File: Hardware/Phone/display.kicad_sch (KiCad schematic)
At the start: 19 parts, among them Q1 Si1308EDL

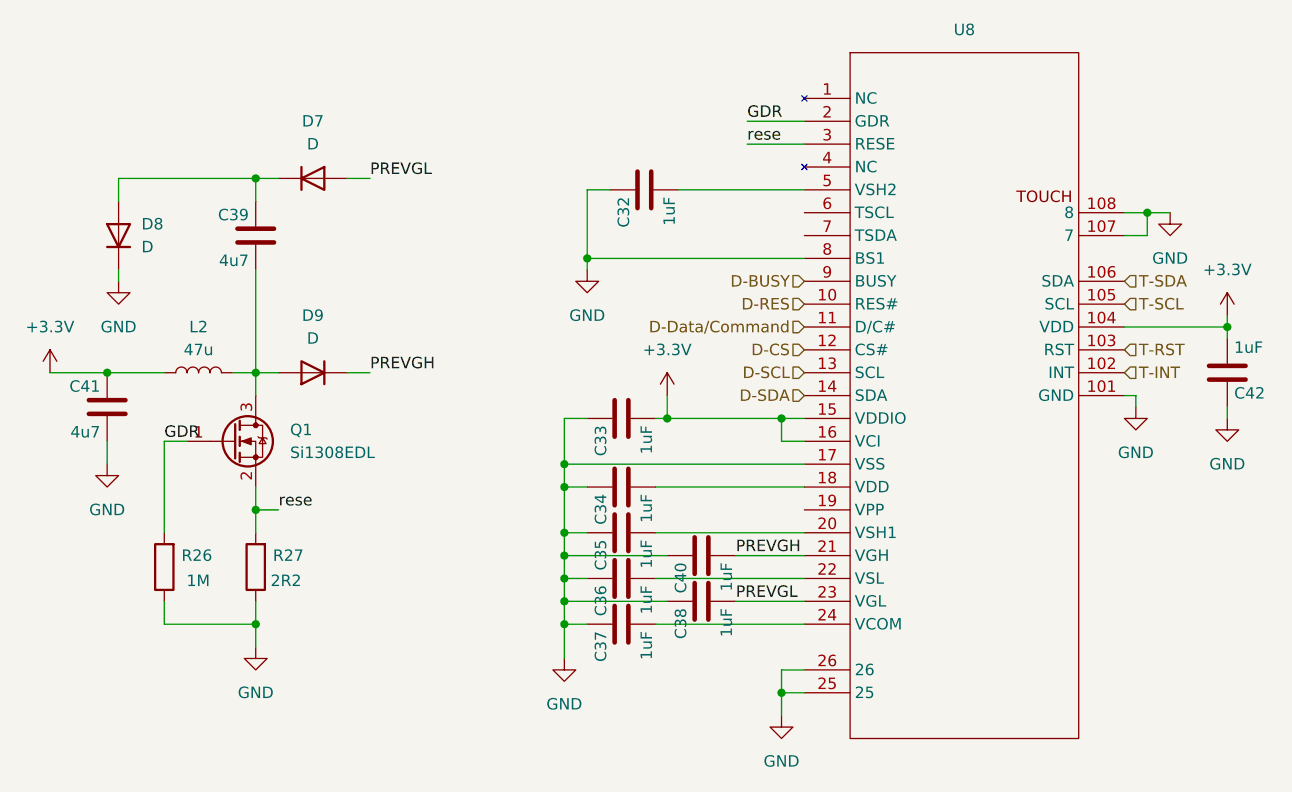
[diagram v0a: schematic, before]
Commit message: phone design is done abendoning projekt
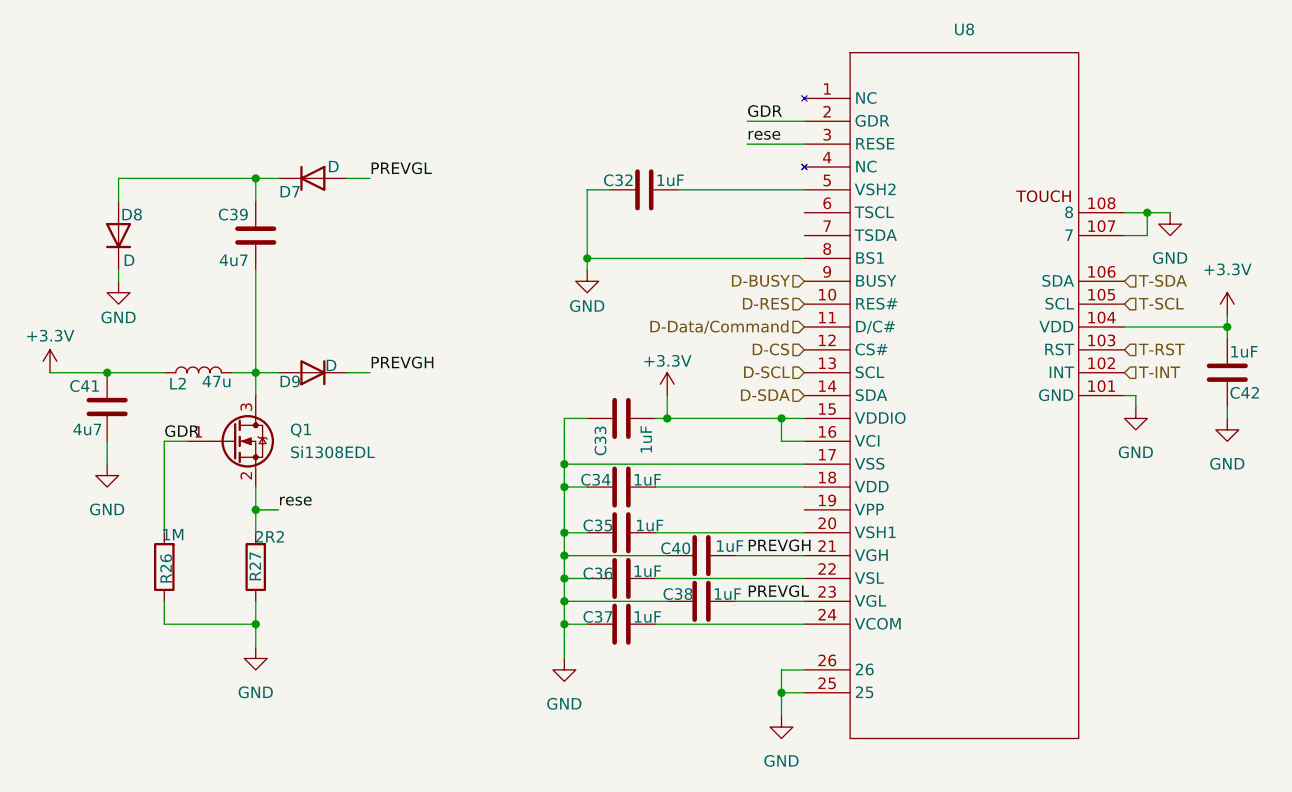
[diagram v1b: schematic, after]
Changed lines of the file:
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@@
+	(wire
+		(pts
+			(xy 125.73 119.38) (xy 133.35 119.38)
+		)
+		(stroke
+			(width 0)
+			(type default)
+		)
+	)
 	(wire
 		(pts
@@
 	(wire
 		(pts
-			(xy 125.73 119.38) (xy 133.35 119.38)
-		)
-		(stroke
-			(width 0)
-			(type default)
-		)
-	)
-	(wire
-		(pts
 			(xy 116.84 116.84) (xy 133.35 116.84)
 		)
@@
 	)
 	(label "PREVGL"
-		(at 125.73 119.38 0)
+		(at 127 119.38 0)
 		(fields_autoplaced yes)
 		(effects
@@
 	)
 	(label "PREVGH"
-		(at 125.73 114.3 0)
+		(at 127 114.3 0)
 		(fields_autoplaced yes)
 		(effects
@@
 		(dnp no)
 		(property "Reference" "R27"
-			(at 77.724 114.3 0)
+			(at 72.39 113.792 90)
 			(effects
 				(font
@@
 		)
 		(property "Value" "2R2"
-			(at 77.47 117.094 0)
+			(at 75.692 112.268 0)
 			(effects
 				(font
@@
 		(on_board yes)
 		(dnp no)
-		(fields_autoplaced yes)
 		(property "Reference" "#PWR061"
 			(at 49.53 97.79 0)
@@
 		)
 		(property "Value" "+3.3V"
-			(at 49.53 88.9 0)
+			(at 49.53 89.916 0)
 			(effects
 				(font
@@
 		(on_board yes)
 		(dnp no)
-		(fields_autoplaced yes)
 		(property "Reference" "#PWR058"
 			(at 118.11 100.33 0)
@@
 		)
 		(property "Value" "+3.3V"
-			(at 118.11 91.44 0)
+			(at 118.11 92.71 0)
 			(effects
 				(font
@@
 		(dnp no)
 		(property "Reference" "R26"
-			(at 67.564 114.3 0)
+			(at 62.484 114.046 90)
 			(effects
 				(font
@@
 		)
 		(property "Value" "1M"
-			(at 67.31 117.094 0)
+			(at 64.516 112.014 0)
 			(effects
 				(font
@@
 		)
 		(property "Value" "4u7"
-			(at 55.118 100.584 0)
+			(at 55.372 100.33 0)
 			(effects
 				(font
@@
 		(on_board yes)
 		(dnp no)
-		(fields_autoplaced yes)
 		(property "Reference" "D7"
-			(at 78.74 66.04 0)
+			(at 76.2 73.914 0)
 			(effects
 				(font
@@
 		)
 		(property "Value" "D"
-			(at 78.74 68.58 0)
+			(at 81.026 71.12 0)
 			(effects
 				(font
@@
 		(on_board yes)
 		(dnp no)
-		(fields_autoplaced yes)
 		(property "Reference" "D8"
-			(at 59.69 77.4699 90)
+			(at 57.404 76.454 90)
 			(effects
 				(font
@@
 		)
 		(property "Value" "D"
-			(at 59.69 80.0099 90)
+			(at 57.658 81.534 90)
 			(effects
 				(font
@@
 		(dnp no)
 		(property "Reference" "C32"
-			(at 113.284 74.422 0)
+			(at 110.998 72.644 90)
 			(effects
 				(font
@@
 		)
 		(property "Value" "1uF"
-			(at 118.364 74.422 0)
+			(at 116.84 72.644 90)
 			(effects
 				(font
@@
 		(on_board yes)
 		(dnp no)
-		(fields_autoplaced yes)
 		(property "Reference" "#PWR059"
 			(at 57.15 90.17 0)
@@
 		)
 		(property "Value" "GND"
-			(at 57.15 88.9 0)
+			(at 57.15 87.884 0)
 			(effects
 				(font
@@
 		(dnp no)
 		(property "Reference" "C38"
-			(at 119.634 120.142 0)
+			(at 117.602 118.618 90)
 			(effects
 				(font
@@
 		)
 		(property "Value" "1uF"
-			(at 124.714 120.142 0)
+			(at 123.19 118.618 90)
 			(effects
 				(font
@@
 		(dnp no)
 		(property "Reference" "C40"
-			(at 119.634 115.062 0)
+			(at 117.348 113.538 90)
 			(effects
 				(font
@@
 		)
 		(property "Value" "1uF"
-			(at 124.714 115.062 0)
+			(at 123.444 113.284 90)
 			(effects
 				(font
@@
 		(on_board yes)
 		(dnp no)
-		(fields_autoplaced yes)
 		(property "Reference" "#PWR056"
 			(at 109.22 88.9 0)
@@
 		)
 		(property "Value" "GND"
-			(at 109.22 87.63 0)
+			(at 109.22 86.614 0)
 			(effects
 				(font
@@
 		(dnp no)
 		(property "Reference" "C36"
-			(at 110.744 117.602 0)
+			(at 108.712 116.332 90)
 			(effects
 				(font
@@
 		)
 		(property "Value" "1uF"
-			(at 115.824 117.602 0)
+			(at 114.3 116.078 90)
 			(effects
 				(font
@@
 		(on_board yes)
 		(dnp no)
-		(fields_autoplaced yes)
 		(property "Reference" "L2"
-			(at 66.04 88.9 90)
+			(at 63.754 95.25 90)
 			(effects
 				(font
@@
 		)
 		(property "Value" "47u"
-			(at 66.04 91.44 90)
+			(at 68.072 94.996 90)
 			(effects
 				(font
@@
 		(dnp no)
 		(property "Reference" "C35"
-			(at 110.744 112.522 0)
+			(at 108.712 110.998 90)
 			(effects
 				(font
@@
 		)
 		(property "Value" "1uF"
-			(at 115.824 112.522 0)
+			(at 114.554 110.998 90)
 			(effects
 				(font
@@
 		(dnp no)
 		(property "Reference" "C42"
-			(at 181.102 96.266 0)
+			(at 180.594 96.266 0)
 			(effects
 				(font
@@
 		)
 		(property "Value" "1uF"
-			(at 181.102 91.186 0)
+			(at 180.594 91.694 0)
 			(effects
 				(font
@@
 		(dnp no)
 		(property "Reference" "C34"
-			(at 110.744 107.442 0)
+			(at 108.458 105.918 90)
 			(effects
 				(font
@@
 		)
 		(property "Value" "1uF"
-			(at 115.824 107.442 0)
+			(at 114.3 105.918 90)
 			(effects
 				(font
@@
 		(dnp no)
 		(property "Reference" "C37"
-			(at 110.744 122.682 0)
+			(at 108.712 121.158 90)
 			(effects
 				(font
@@
 		)
 		(property "Value" "1uF"
-			(at 115.824 122.682 0)
+			(at 114.3 121.158 90)
 			(effects
 				(font
@@
 		(on_board yes)
 		(dnp no)
-		(fields_autoplaced yes)
 		(property "Reference" "D9"
-			(at 78.74 87.63 0)
+			(at 76.2 94.996 0)
 			(effects
 				(font
@@
 		)
 		(property "Value" "D"
-			(at 78.74 90.17 0)
-			(effects
-				(font
+			(at 80.772 93.218 0)
+			(effects
+				(font

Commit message: added doku. Abendoning Projekt
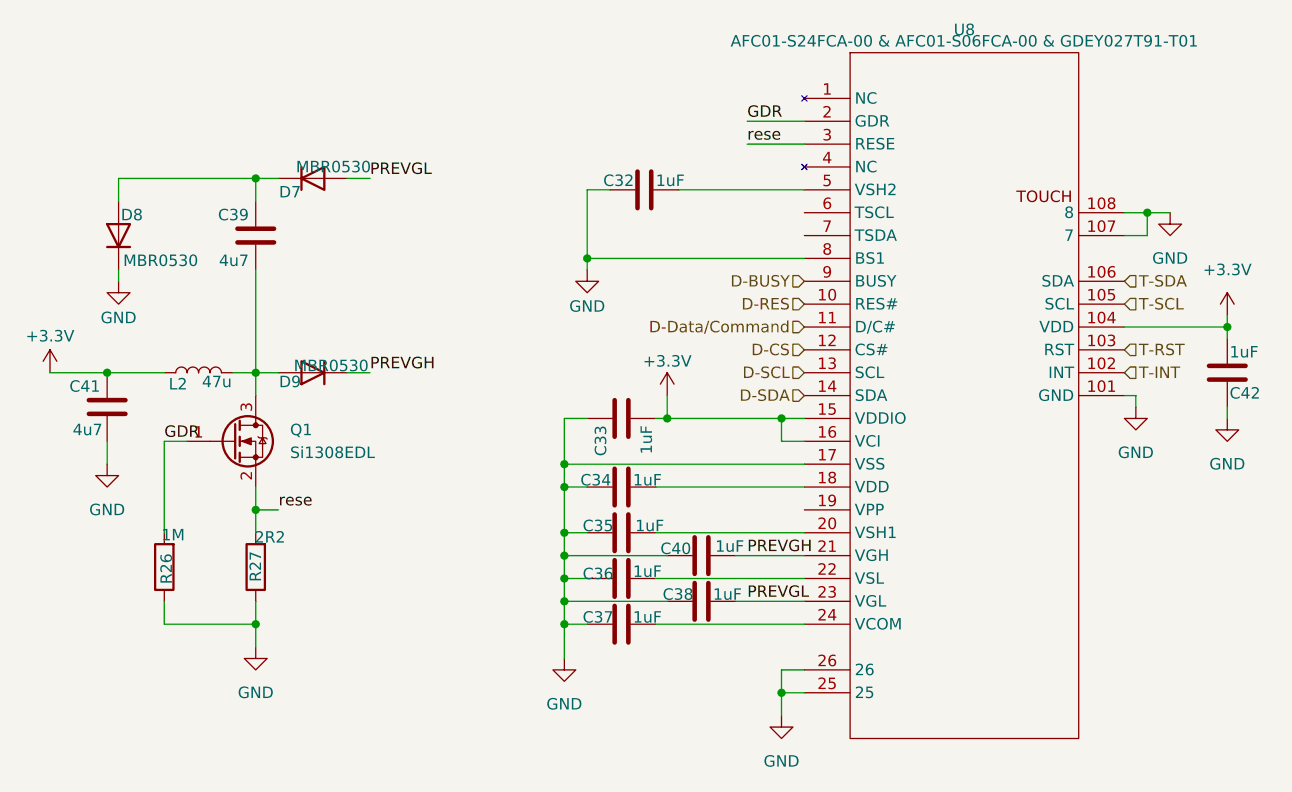
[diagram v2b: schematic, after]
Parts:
- D7, D8, D9: value D -> MBR0530
- U8: value ~ -> AFC01-S24FCA-00 & AFC01-S06FCA-00 & GDEY027T91-T01
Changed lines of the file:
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@@
 			)
 		)
-		(property "Value" "D"
+		(property "Value" "MBR0530"
 			(at 81.026 71.12 0)
 			(effects
@@
 			)
 		)
-		(property "Value" "D"
+		(property "Value" "MBR0530"
 			(at 57.658 81.534 90)
 			(effects
@@
 			)
 		)
-		(property "Value" "~"
+		(property "Value" "AFC01-S24FCA-00  & AFC01-S06FCA-00 & GDEY027T91-T01"
 			(at 151.13 57.15 0)
 			(effects
@@
 			)
 		)
-		(property "Value" "D"
+		(property "Value" "MBR0530"
 			(at 80.772 93.218 0)
 			(effects
